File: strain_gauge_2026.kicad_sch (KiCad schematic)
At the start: 22 parts, among them J2 Conn_01x04_Socket, J3 Conn_01x04_Socket, J5 Conn_01x04_Socket, U1 NAU7802SGI

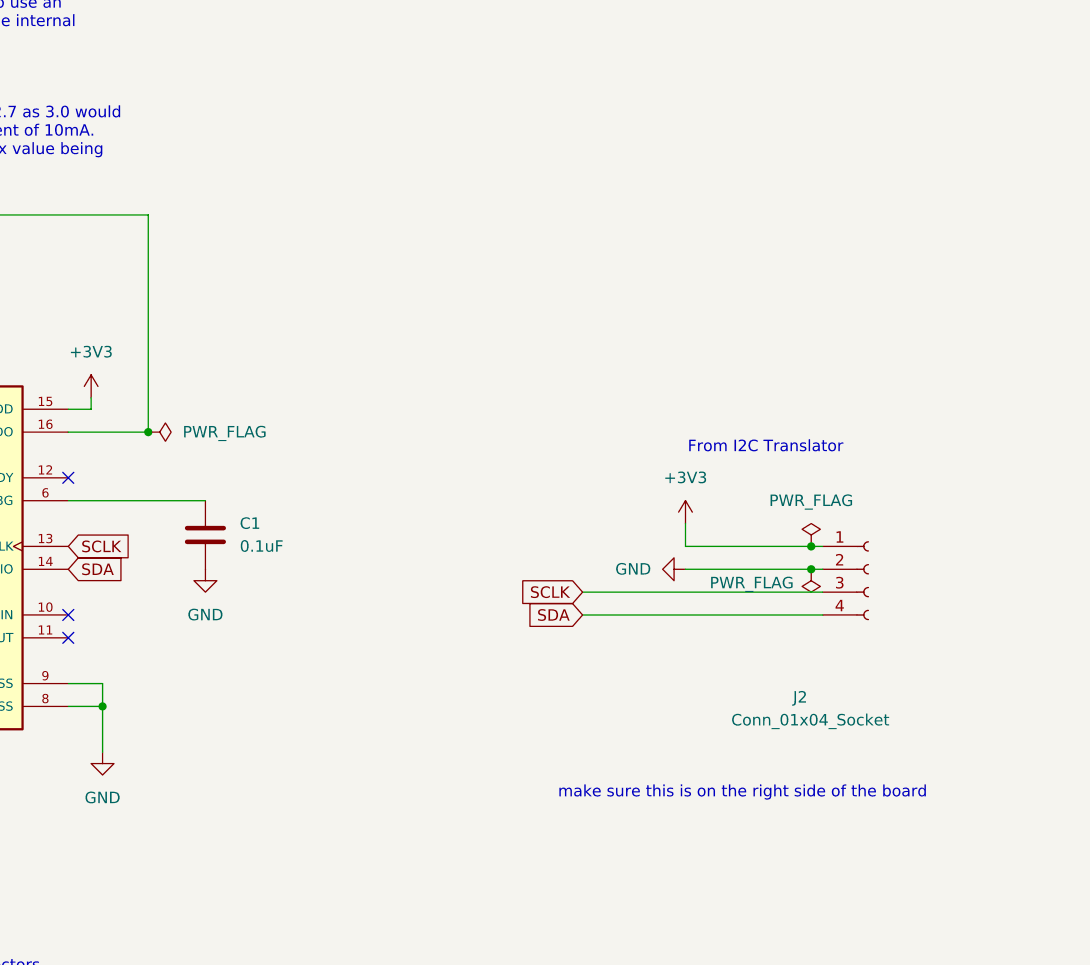
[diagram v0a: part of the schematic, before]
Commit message: Added DFR1193 to Schematic and PCB Layout
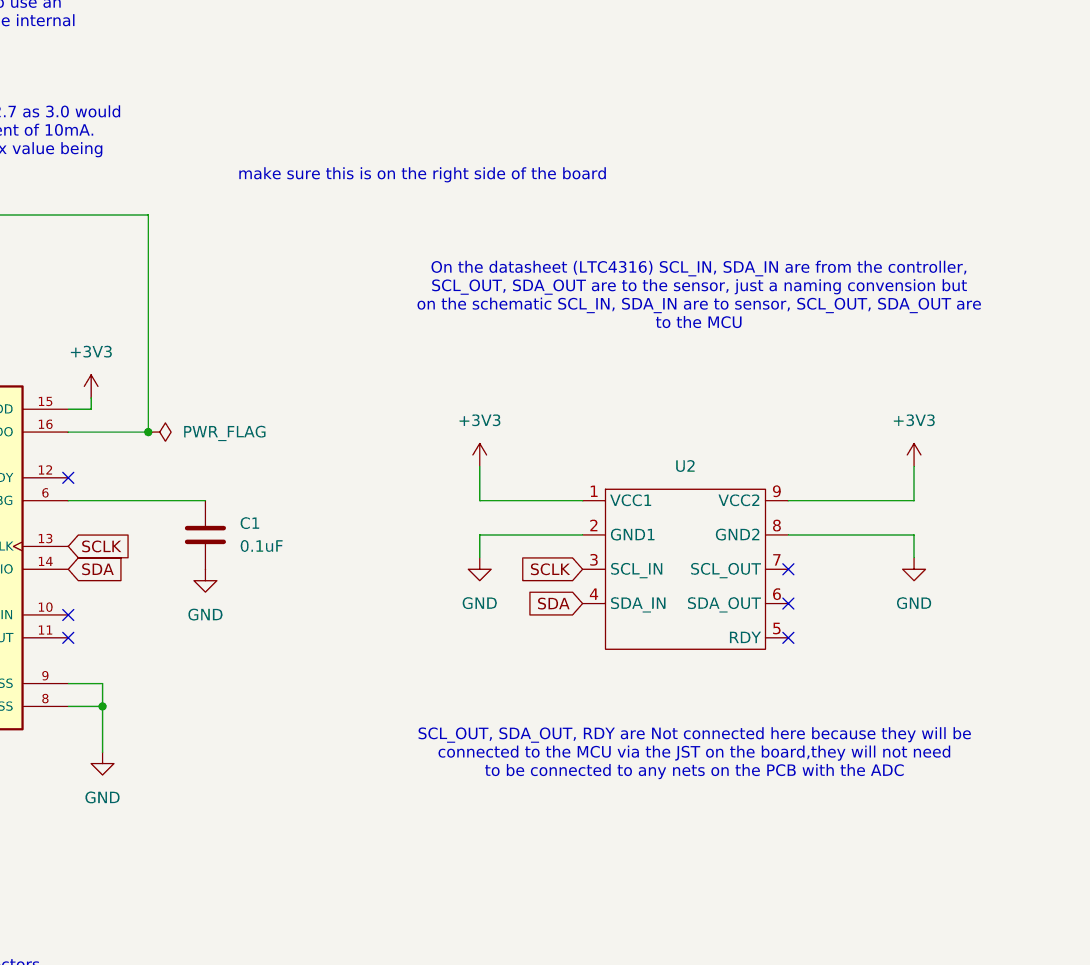
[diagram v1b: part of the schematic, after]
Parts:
- removed J2: Conn_01x04_Socket, Connector_PinHeader_2.54mm:PinHeader_1x04_P2.54mm_Vertical, symbol Connector:Conn_01x04_Socket
- added U2: (no value), strain_gauge_footprint_lib:DFR1193, symbol strain_gauge_library:DFR1193
- C6: footprint Capacitor_THT:CP_Radial_D5.0mm_P2.00mm -> Capacitor_SMD:C_0805_2012Metric_Pad1.18x1.45mm_HandSolder
- C9: footprint Capacitor_THT:C_Rect_L7.0mm_W3.5mm_P5.00mm -> Capacitor_SMD:C_0805_2012Metric_Pad1.18x1.45mm_HandSolder
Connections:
- net +3V3: now also U2.1 (VCC1), U2.9 (VCC2)
- net GND: now also U2.2 (GND1), U2.8 (GND2)
- net SCLK: now also U2.3 (SCL_IN)
- net SDA: now also U2.4 (SDA_IN)
- no-connect marks 3 -> 6
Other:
- note added: "On the datasheet (LTC4316) SCL_IN, SDA_IN are from the controller, SCL_OUT, SDA_OUT are to the sensor, just a naming convension but on the schematic SCL_IN, SDA_IN are to sensor, SCL_OUT, SDA_OUT are to the MCU"
- note added: "SCL_OUT, SDA_OUT, RDY are Not connected here because they will be connected to the MCU via the JST on the board,they will not need to be connected to any nets on the PCB with the ADC"
- note removed: "From I2C Translator"

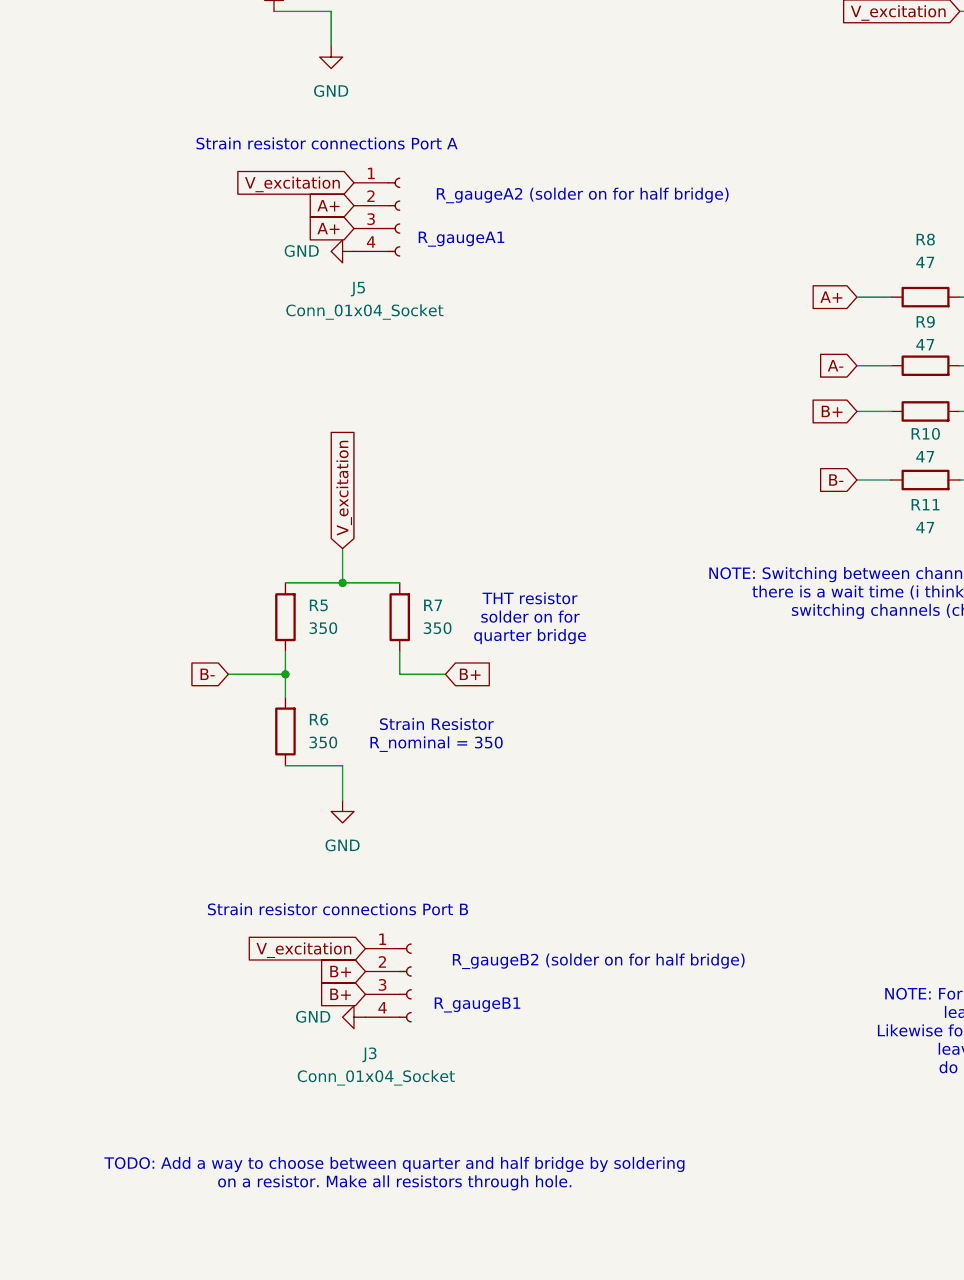
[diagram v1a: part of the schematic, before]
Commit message: Changed 2x4pin JST connectors for strain resistors to 4x2pin connectors
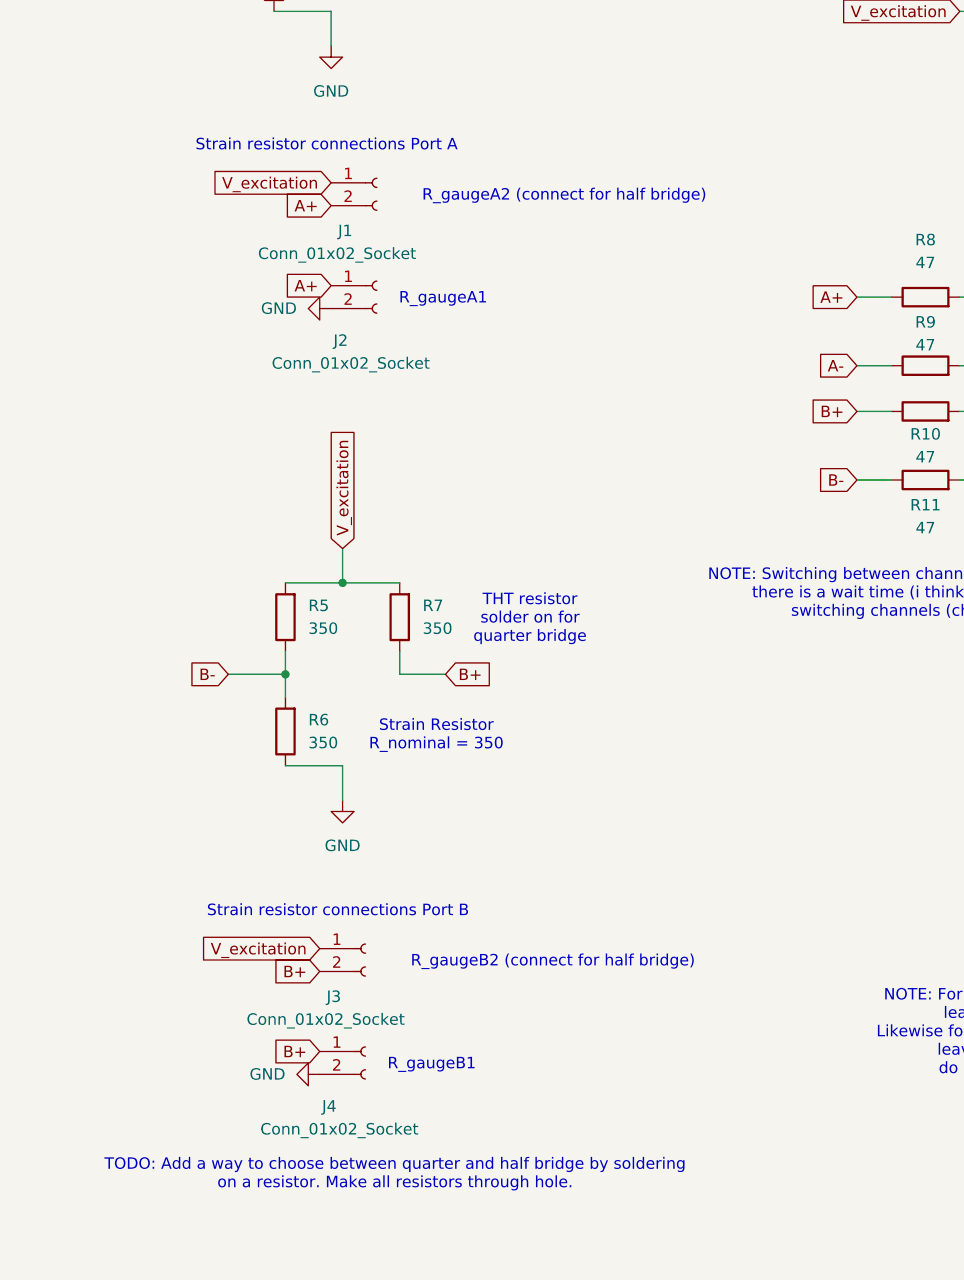
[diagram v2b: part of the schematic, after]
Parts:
- removed J3, J5: Conn_01x04_Socket, Connector_PinHeader_2.54mm:PinHeader_1x04_P2.54mm_Vertical, symbol Connector:Conn_01x04_Socket
- added J1, J2, J3, J4: Conn_01x02_Socket, Connector_PinHeader_2.54mm:PinHeader_1x02_P2.54mm_Vertical, symbol Connector:Conn_01x02_Socket
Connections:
- net A+: now also J1.2 (Pin_2), J2.1 (Pin_1)
- net B+: now also J3.2 (Pin_2), J4.1 (Pin_1)
- net GND: now also J2.2 (Pin_2), J4.2 (Pin_2)
- net V_excitation: now also J1.1 (Pin_1), J3.1 (Pin_1)
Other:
- note added: "R_gaugeA2 (connect for half bridge)"
- note added: "R_gaugeB2 (connect for half bridge)"
- note removed: "R_gaugeA2 (solder on for half bridge)"
- note removed: "R_gaugeB2 (solder on for half bridge)"
